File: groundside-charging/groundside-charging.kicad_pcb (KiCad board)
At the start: 2 copper layers, 45.2 x 70.6 mm, 29 parts, among them J1 12V In, J2 Charge Current Out (to Rocket), J3 Charge Voltage Sensing, Q1 SI4840BDY-T1-GE3, U1 LM317DCYR, U2 LM3478MA

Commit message: address tessa feedback
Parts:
- C2, C3: value 68uF -> 68u
- C4: value 100nF -> 100n
- C5: value 820pF -> 820p
- C6: value 15nF -> 15n
- C7: value 10pF -> 10p
- Q1: footprint groundside-charging:SO-8-SINGLE_MS-012_VIS -> groundside-charging:SI4840BDY-T1-GE3
- R5: value 10mR -> 15m
- U1: footprint Package_TO_SOT_SMD:SOT-223-3_TabPin2 -> groundside-charging:LM317DCYR
- moved U1 3.85 mm to (102.2, 116.6), turned to 180 degrees
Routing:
- net Net-(U1-VO): track 18.2 -> 6.30 mm, vias 0 -> 10
- net Net-(Q1-G): track 12.5 -> 11.8 mm
- added copper zone on B.Cu, net Net-(U1-VO)
- added copper zone on F.Cu, net Net-(U1-VO)
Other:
- board size 45.2 x 70.6 mm -> 45.7 x 71.1 mm
- board text added: "eat hot chip/charge rocket/lie Ash Lang May 2025"
- board text removed: "eat hot chip/charge rocket/lie Ash L May 2025"

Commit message: generate gerbs, pdf
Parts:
- added G***: LOGO, groundside-charging:Logo_SilkScreen_5mm, F.Cu at (68.8, 151.6)
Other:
- board text added: "I_{out}"
- board text added: "V_{sense}"
- board text removed: "+CHG"
- board text removed: "V_{out}"

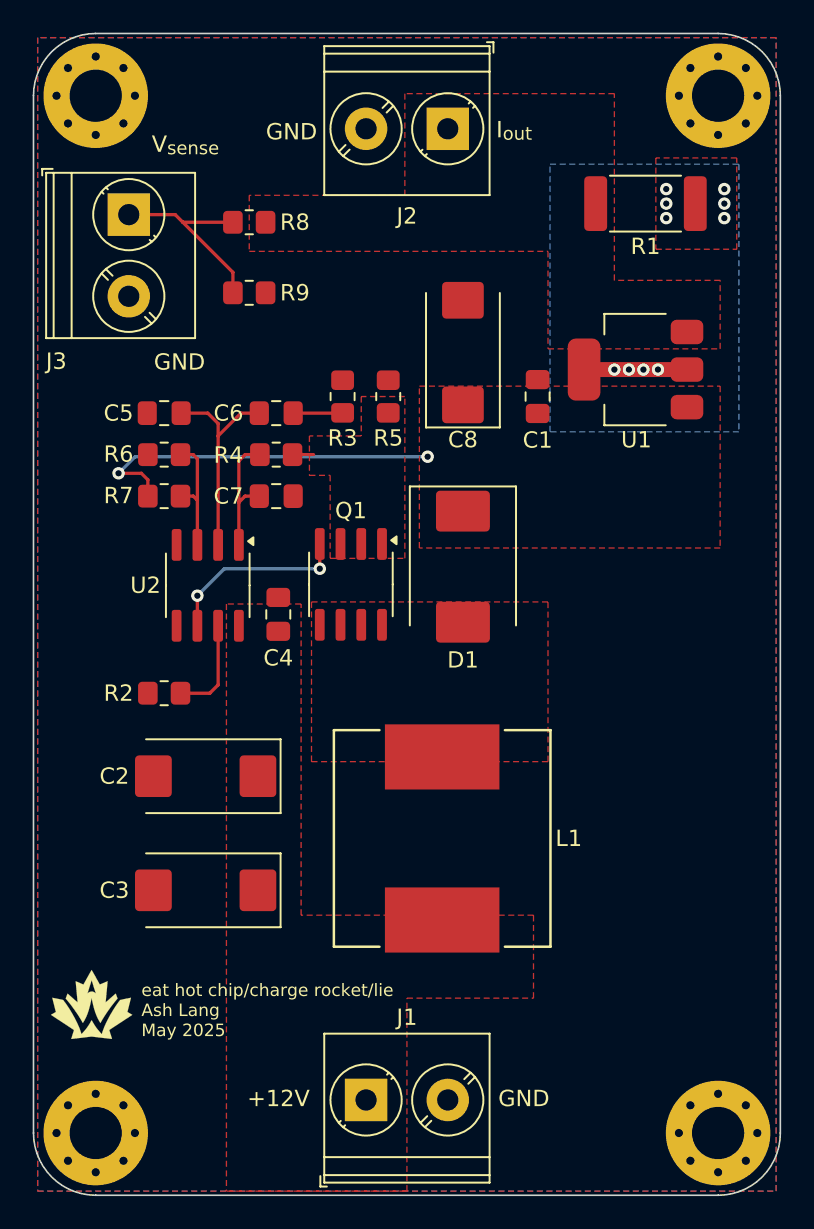
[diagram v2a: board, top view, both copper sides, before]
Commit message: select components and layout/route
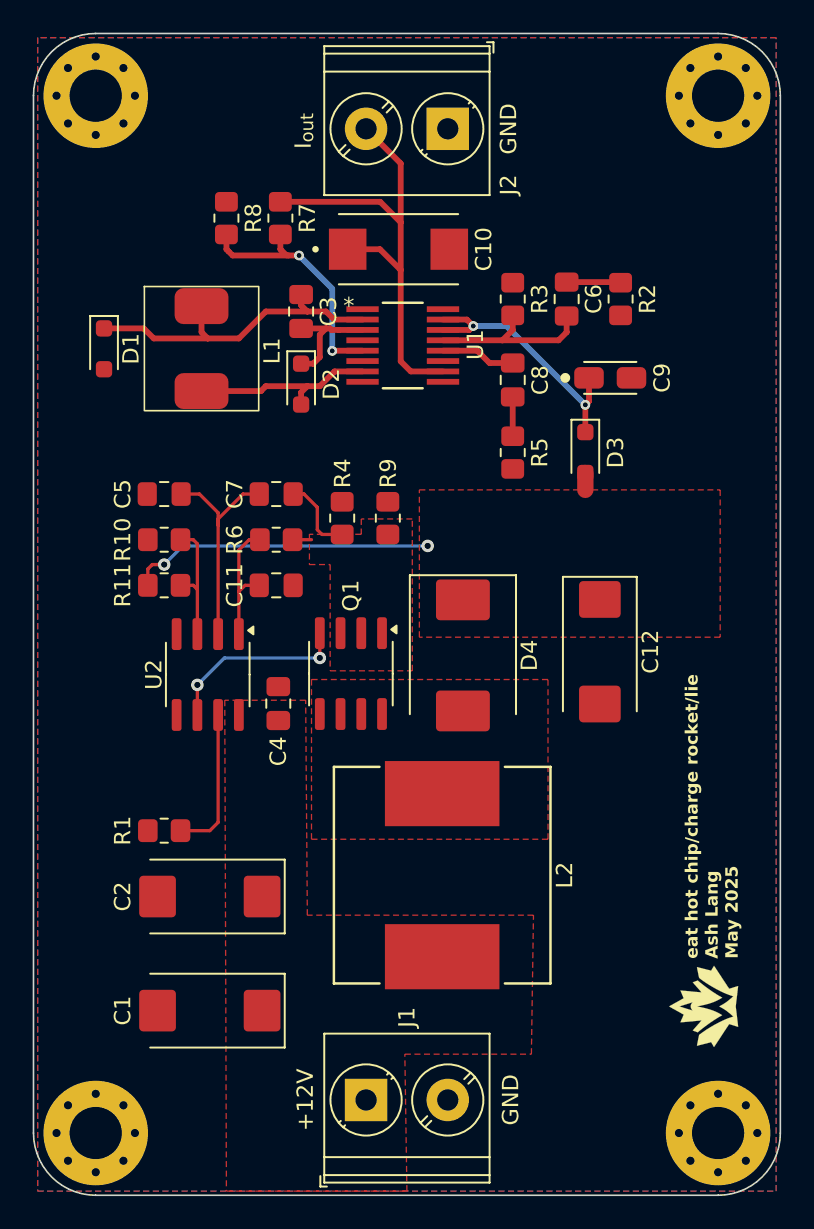
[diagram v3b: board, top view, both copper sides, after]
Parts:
- removed J3: Charge Voltage Sensing, TerminalBlock_Phoenix:TerminalBlock_Phoenix_PT-1,5-2-5.0-H_1x02_P5.00mm_Horizontal
- added C10: TCJB226M025R0150, groundside-charging:CAPPM7343X310N, F.Cu at (87.6, 105.4)
- added C11: 10p, Capacitor_SMD:C_0805_2012Metric_Pad1.18x1.45mm_HandSolder, F.Cu at (80.1, 126.0)
- added C12: 150uF, Capacitor_Tantalum_SMD:CP_EIA-7343-31_Kemet-D_Pad2.25x2.55mm_HandSolder, F.Cu at (99.9, 130.0)
- added C9: TCJA106M025R0150, groundside-charging:CAPPM3216X180N, F.Cu at (100.6, 113.3)
- added D2: BAS316,115, Diode_SMD:D_SOD-323_HandSoldering, F.Cu at (81.7, 113.7)
- added D3: CUS10S30,H3F, Diode_SMD:D_SOD-323_HandSoldering, F.Cu at (99.1, 117.9)
- added D4: B540C-13-F, Diode_SMD:D_SMC, F.Cu at (91.6, 130.3)
- added L2: SRR1208-100ML, groundside-charging:IND_BOURNS_SRR1208, F.Cu at (90.3, 143.7)
- added R10: 1k, Resistor_SMD:R_0805_2012Metric_Pad1.20x1.40mm_HandSolder, F.Cu at (73.3, 123.2)
- added R11: 13.3k, Resistor_SMD:R_0805_2012Metric_Pad1.20x1.40mm_HandSolder, F.Cu at (73.3, 126.0)
- C1: value 0.1uF -> 68u; footprint Capacitor_SMD:C_0805_2012Metric_Pad1.18x1.45mm_HandSolder -> Capacitor_Tantalum_SMD:CP_EIA-7343-31_Kemet-D_Pad2.25x2.55mm_HandSolder
- C3: value 68u -> 0.22uF; footprint Capacitor_Tantalum_SMD:CP_EIA-7343-31_Kemet-D_Pad2.25x2.55mm_HandSolder -> Capacitor_SMD:C_0805_2012Metric_Pad1.18x1.45mm_HandSolder
- C6: value 15n -> 1uF
- C7: value 10p -> 15n
- C8: value 150uF -> 0.1uF; footprint Capacitor_Tantalum_SMD:CP_EIA-7343-31_Kemet-D_Pad2.25x2.55mm_HandSolder -> Capacitor_SMD:C_0805_2012Metric_Pad1.18x1.45mm_HandSolder
- D1: value B540C-13-F -> CUS10S30,H3F; footprint Diode_SMD:D_SMC -> Diode_SMD:D_SOD-323_HandSoldering
- L1: value SRR1208-100ML -> HCMA0703-330-R; footprint groundside-charging:IND_BOURNS_SRR1208 -> groundside-charging:HCMA0703-330-R
- R1: value 1.25R -> 34k; footprint Resistor_SMD:R_2512_6332Metric_Pad1.40x3.35mm_HandSolder -> Resistor_SMD:R_0805_2012Metric_Pad1.20x1.40mm_HandSolder
- R2: value 34k -> 300R
- R3: value 4.99k -> 4.93k
- R4: value 100R -> 4.99k
- R5: value 15m -> 1k
- R6: value 1k -> 100R
- R7: value 13.3k -> 75k
- R8: value TBD -> 18k
- R9: value TBD -> 15m
- U1: value LM317DCYR -> LT1510-5IGN_PBF; footprint groundside-charging:LM317DCYR -> groundside-charging:SSOP-16_GN
- moved R1 48.4 mm to (73.3, 141.0)
- moved C1 42.6 mm to (76.1, 152.0), turned to 180 degrees
- moved G*** 37.5 mm to (106.3, 151.8), turned to 90 degrees
- moved R2 36.9 mm to (101.2, 108.5), turned to -90 degrees
- moved L1 36.9 mm to (75.6, 107.7), turned to 0 degrees
- moved C3 35.9 mm to (81.7, 109.2), turned to -90 degrees
- moved D1 25.7 mm to (69.6, 111.5)
- moved C6 19.1 mm to (97.9, 108.5), turned to 90 degrees
- moved R7 18.4 mm to (80.4, 103.5), turned to -90 degrees
- moved R9 16.2 mm to (87.0, 121.9), turned to -90 degrees
- moved U1 15.2 mm to (87.9, 111.3), turned to 0 degrees
- moved R3 12.0 mm to (94.6, 108.5)
- moved R6 8.61 mm to (80.1, 123.2), turned to 0 degrees
- moved R5 8.36 mm to (94.6, 117.9)
- moved C2 7.37 mm to (76.1, 145.0)
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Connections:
- C1 pad 1: +18V -> +12V
- C3 pad 1: +12V -> Net-(D1-K)
- C3 pad 2: GND -> Net-(D2-K)
- C6 pad 1: Net-(U2-COMP) -> /PROG
- C7 pad 1: Net-(U2-I_{SEN}) -> Net-(U2-COMP)
- C7 pad 2: GND -> Net-(C7-Pad2)
- C8 pad 1: +18V -> /VC
- C8 pad 2: GND -> Net-(C8-Pad2)
- D1 pad 1: +18V -> Net-(D1-K)
- D1 pad 2: Net-(D1-A) -> GND
- J2 pad 1: VCC -> GND
- J2 pad 2: GND -> VCC
- L1 pad 1: +12V -> Net-(D1-K)
- L1 pad 2: Net-(D1-A) -> Net-(D2-A)
- Q1 pad 1: Net-(D1-A) -> Net-(D4-A)
- R1 pad 1: Net-(U1-VO) -> Net-(U2-FA/SD)
- R1 pad 2: VCC -> GND
- R2 pad 1: Net-(U2-FA/SD) -> Net-(C6-Pad2)
- R3 pad 1: Net-(C6-Pad2) -> /PROG
- R4 pad 1: Net-(U2-I_{SEN}) -> Net-(C7-Pad2)
- R4 pad 2: Net-(Q1-S) -> GND
- R5 pad 1: GND -> Net-(C8-Pad2)
- R5 pad 2: Net-(Q1-S) -> GND
- R6 pad 1: /FB -> Net-(U2-I_{SEN})
- R6 pad 2: GND -> Net-(Q1-S)
- R7 pad 1: /FB -> VCC
- R7 pad 2: +18V -> /OVP
- R8 pad 1: VCC -> /OVP
- R8 pad 2: Net-(J3-Pin_1) -> GND
- R9 pad 1: Net-(J3-Pin_1) -> GND
- R9 pad 2: GND -> Net-(Q1-S)
- U1 pad 1: VCC -> GND
- U1 pad 2: Net-(U1-VO) -> Net-(D1-K)
- U1 pad 3: +18V -> Net-(D2-K)
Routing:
- net VCC: track 0.00 -> 29.6 mm
- net Net-(D1-K): track 0.00 -> 20.3 mm
- net Net-(D3-K): track 0.00 -> 16.2 mm, vias 0 -> 2
- net /OVP: track 0.00 -> 15.5 mm, vias 0 -> 2
- net Net-(J3-Pin_1): track 12.2 -> 0.00 mm
- net Net-(D2-A): track 0.00 -> 11.6 mm
- net /PROG: track 0.00 -> 10.6 mm
- net Net-(D2-K): track 0.00 -> 7.02 mm
- net Net-(U1-VO): track 6.30 -> 0.00 mm, vias 10 -> 0
- net Net-(C7-Pad2): track 0.00 -> 4.83 mm
- net /VC: track 0.00 -> 4.58 mm
- net Net-(U2-FA/SD): track 6.13 -> 9.09 mm
- net +18V: track 22.3 -> 19.8 mm
- net Net-(C8-Pad2): track 0.00 -> 2.41 mm
- net Net-(U2-COMP): track 13.1 -> 13.7 mm
- added copper zone on F.Cu, net Net-(D4-A)
- removed copper zone on F.Cu, net Net-(D1-A)
- removed copper zone on B.Cu, net Net-(U1-VO)
- removed copper zone on F.Cu, net Net-(U1-VO)
- removed copper zone on F.Cu, net VCC
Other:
- board text removed: "V_{sense}"
